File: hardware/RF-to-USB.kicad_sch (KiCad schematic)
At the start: 21 parts, among them J1 USB_A, J2 Conn_Coaxial, J3 ARM SWD, U1 nRF24L01P, U2 STM32L432KBUx, U3 XC6206P332MR, U4 USBLC6-2SC6

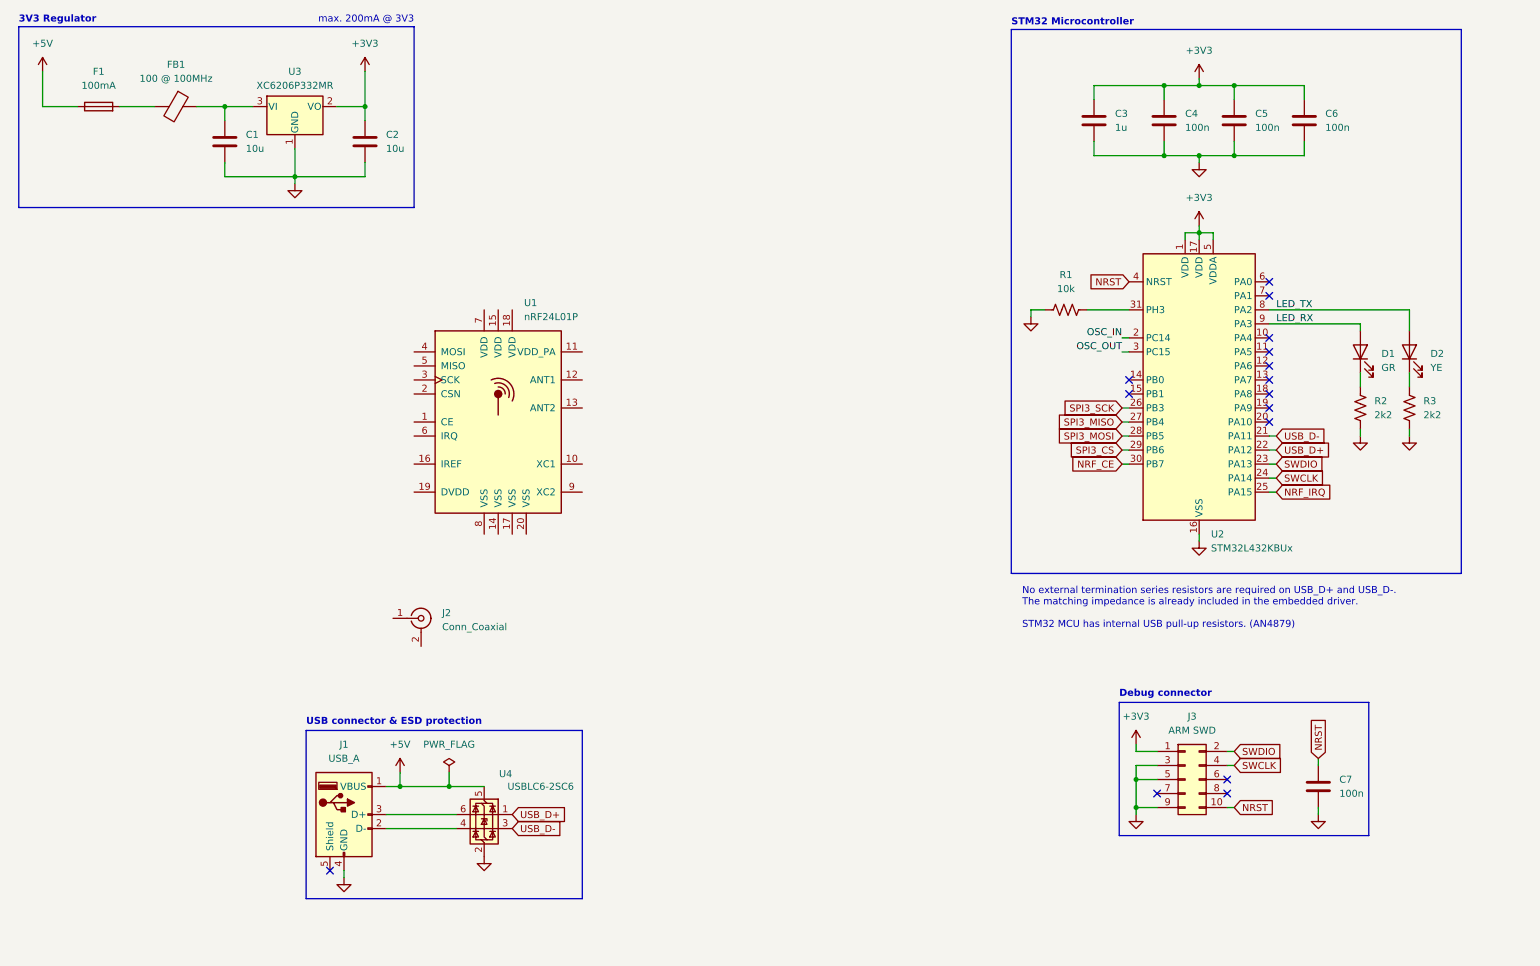
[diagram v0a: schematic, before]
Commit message: NRF24 transceiver schematic
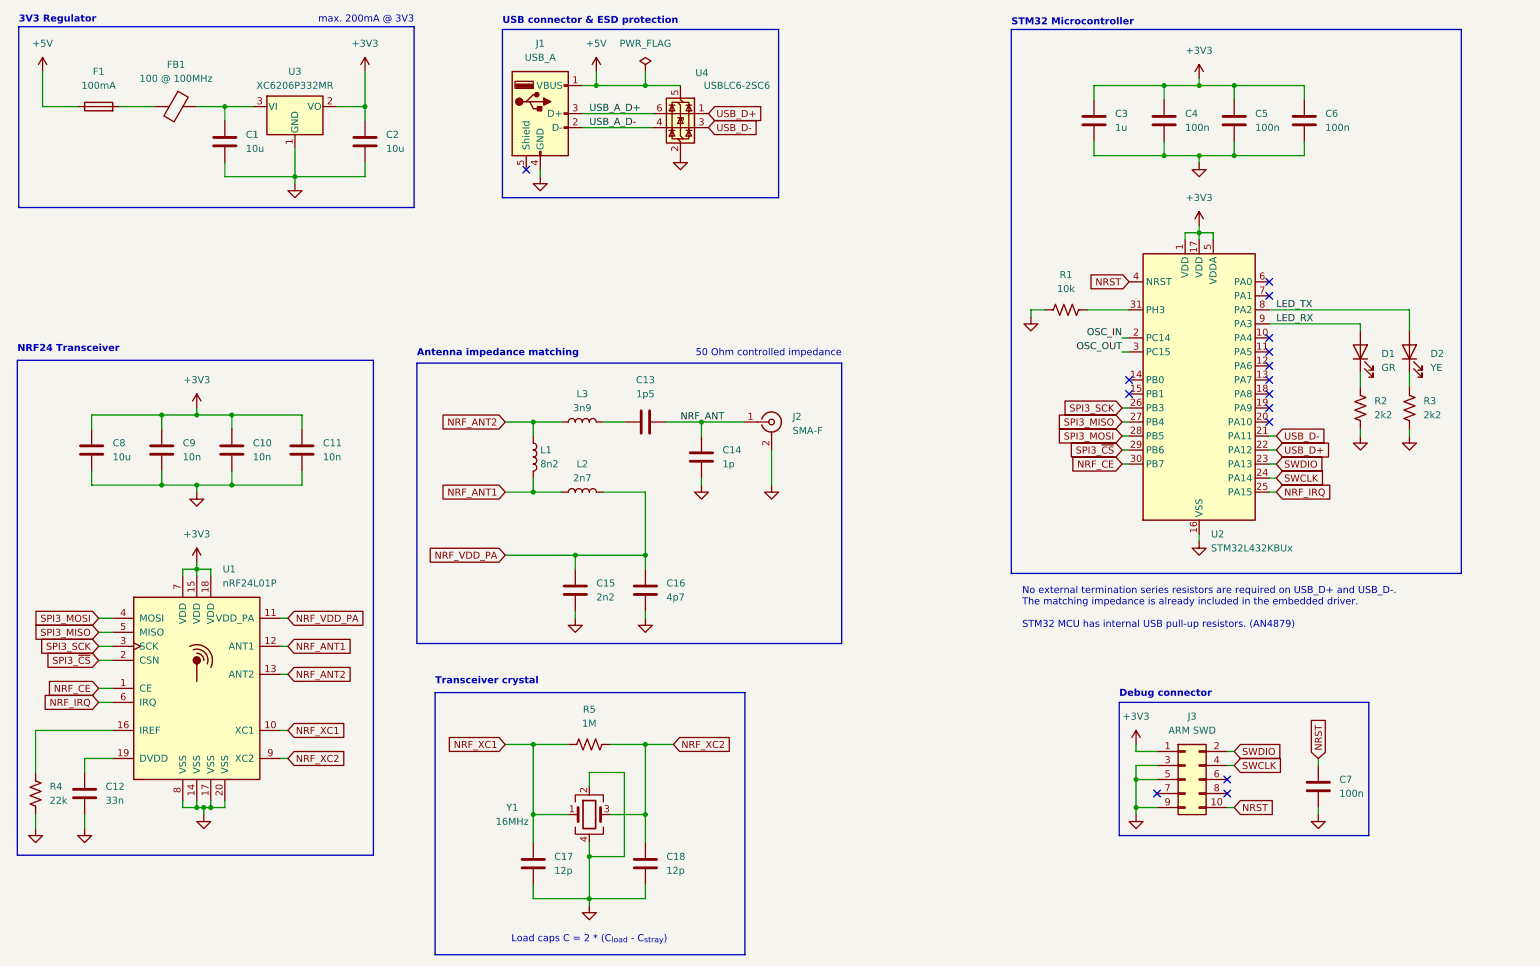
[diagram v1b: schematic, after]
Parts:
- added C10, C11, C9: 10n, symbol Device:C
- added C12: 33n, symbol Device:C
- added C13: 1p5, symbol Device:C
- added C14: 1p, symbol Device:C
- added C15: 2n2, symbol Device:C
- added C16: 4p7, symbol Device:C
- added C17, C18: 12p, symbol Device:C
- added C8: 10u, symbol Device:C
- added L1: 8n2, symbol Device:L
- added L2: 2n7, symbol Device:L
- added L3: 3n9, symbol Device:L
- added R4: 22k, symbol Device:R_US
- added R5: 1M, symbol Device:R_US
- added Y1: 16MHz, Crystal:Crystal_SMD_SeikoEpson_TSX3225-4Pin_3.2x2.5mm, symbol Device:Crystal_GND24
- J2: value Conn_Coaxial -> SMA-F
- U4: Digi-Key (none) -> 497-5235-1-ND; SKU (none) -> USBLC6-2SC6
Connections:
- net SPI3_CS is gone; now on net SPI3_~{CS}: U2.29 (PB6)
- net +3V3: now also U1.15 (VDD), U1.18 (VDD), U1.7 (VDD), C10.1, C11.1, C8.1, C9.1
- net GND: now also J2.2 (Ext), U1.14 (VSS), U1.17 (VSS), U1.20 (VSS), U1.8 (VSS), C10.2, C11.2, C12.2, C14.2, C15.2, C16.2, C17.2, C18.2, C8.2, C9.2, R4.2, Y1.2, Y1.4
- net NRF_CE: now also U1.1 (CE)
- net NRF_IRQ: now also U1.6 (IRQ)
- net SPI3_MISO: now also U1.5 (MISO)
- net SPI3_MOSI: now also U1.4 (MOSI)
- net SPI3_SCK: now also U1.3 (SCK)
- net USB_A_D-: now reaches J1.2 (D-), U4.4 (I/O2)
- net USB_A_D+: now reaches J1.3 (D+), U4.6 (I/O1)
- net NRF_XC1: now reaches U1.10 (XC1)
- net NRF_XC1: now also C17.1, R5.1, Y1.1
- net NRF_VDD_PA: now reaches U1.11 (VDD_PA)
- net NRF_VDD_PA: now also C15.1, C16.1, L2.2
- net NRF_ANT1: now reaches U1.12 (ANT1)
- net NRF_ANT1: now also L1.2, L2.1
- net NRF_ANT2: now reaches U1.13 (ANT2)
- net NRF_ANT2: now also L1.1, L3.1
- net at U1.16 (IREF): now also R4.1
- net at U1.19 (DVDD): now also C12.1
- net SPI3_~{CS}: now reaches U1.2 (CSN)
- net NRF_XC2: now reaches U1.9 (XC2)
- net NRF_XC2: now also C18.1, R5.2, Y1.3
- net NRF_ANT: now reaches J2.1 (In)
- net NRF_ANT: now also C13.2, C14.1
- new net: C13.1, L3.2
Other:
- note added: "50 Ohm controlled impedance"
- note added: "Antenna impedance matching"
- note added: "Load caps C = 2 * (C_{load} - C_{stray})"
- note added: "NRF24 Transceiver"
- note added: "Transceiver crystal"
- moved on the sheet: J1, J2, U1, U4

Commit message: display footprint
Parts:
- added SW1: BTN1, RF-to-USB:Button_TL3301CF260QG, symbol Switch:SW_Push_Dual
- added SW2: BTN2, RF-to-USB:Button_TL3301CF260QG, symbol Switch:SW_Push_Dual
- added U5: OLED, RF-to-USB:Display_Fermion_OLED_128_32, symbol RF-to-USB:OLED_128_32
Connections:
- net +3V3: now also U5.1 (VCC)
- net GND: now also U5.2 (GND)
- net BTN1_EXTI: now reaches U2.12 (PA6)
- net BTN2_EXTI: now reaches U2.13 (PA7)
- net I2C_SCL: now reaches U2.19 (PA9)
- net I2C_SCL: now also U5.3 (SCL)
- net I2C_SDA: now reaches U2.20 (PA10)
- net I2C_SDA: now also U5.4 (SDA)
- no-connect marks 15 -> 11
